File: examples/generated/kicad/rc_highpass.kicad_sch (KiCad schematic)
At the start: 3 parts

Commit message: Attempt to create legible symbols.
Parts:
- C1: symbol examples:CAP -> CAP
- R1: symbol examples:R -> R
- V1: symbol examples:VSOURCE -> VSOURCE
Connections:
- net GND: now also R1.2, V1.1 (E1)
- new net: C1.1, V1.2 (E2)
- new net: C1.2, R1.1
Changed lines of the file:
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@@
     (comment 1 "Generated by mixedsig2cad")
   )
-  (symbol (lib_id "examples:VSOURCE") (at 50.00 55.00 0) (unit 1)
+  (symbol (lib_id "VSOURCE") (at 50.00 55.00 0) (unit 1)
     (in_bom yes) (on_board yes)
     (property "Reference" "V1" (at 50.0 51.19 0)
@@
     )
   )
-  (symbol (lib_id "examples:CAP") (at 95.00 55.00 90) (unit 1)
+  (symbol (lib_id "CAP") (at 95.00 55.00 90) (unit 1)
     (in_bom yes) (on_board yes)
     (property "Reference" "C1" (at 95.0 51.19 0)
@@
     )
   )
-  (symbol (lib_id "examples:R") (at 95.00 90.00 90) (unit 1)
+  (symbol (lib_id "R") (at 95.00 90.00 90) (unit 1)
     (in_bom yes) (on_board yes)
     (property "Reference" "R1" (at 95.0 86.19 0)
@@
     )
   )
-  (symbol (lib_id "examples:GND") (at 38.00 41.38 0) (unit 1)
+  (symbol (lib_id "GND") (at 38.00 41.38 0) (unit 1)
     (in_bom yes) (on_board yes)
     (property "Reference" "#PWR0001" (at 38.0 37.57 0)

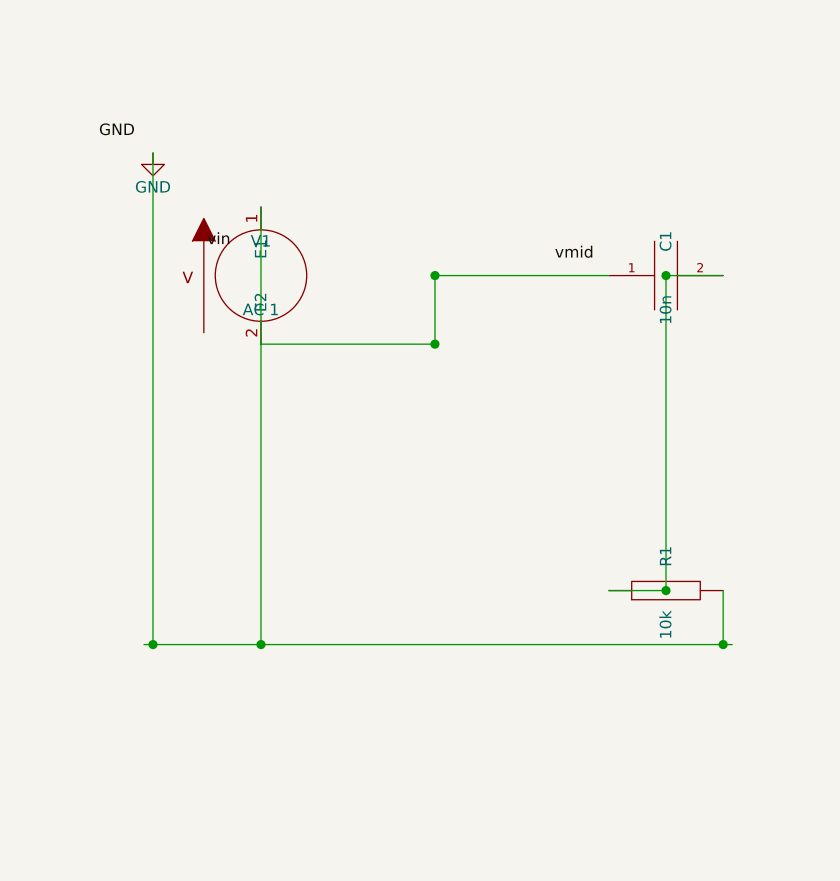
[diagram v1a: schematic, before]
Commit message: Attempt full seperation of circuit concerns into layers.
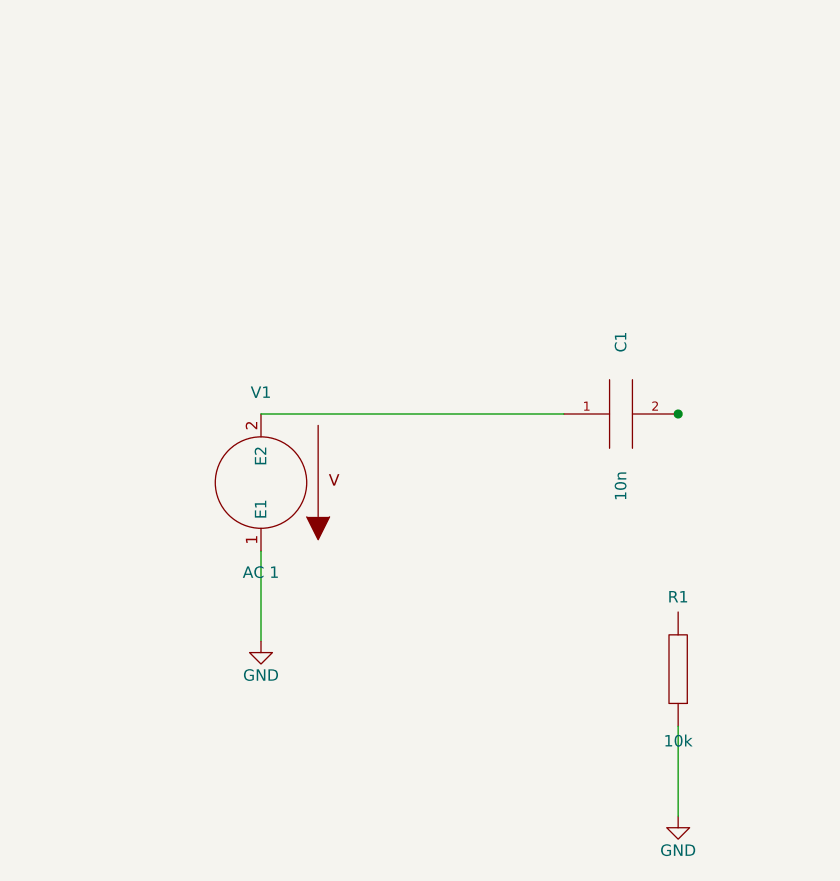
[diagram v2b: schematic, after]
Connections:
- net GND: now also R1.1; no longer R1.2
- net at C1.2: no longer R1.1
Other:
- moved on the sheet: C1, R1, V1
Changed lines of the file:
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@@
   (title_block
     (title "rc_highpass")
-    (date "2026-03-05")
+    (date "2026-03-06")
     (comment 1 "Generated by mixedsig2cad")
   )
-  (symbol (lib_id "VSOURCE") (at 50.00 55.00 0) (unit 1)
+  (symbol (lib_id "VSOURCE") (at 50.00 78.00 180) (unit 1)
     (in_bom yes) (on_board yes)
-    (property "Reference" "V1" (at 50.0 51.19 0)
+    (property "Reference" "V1" (at 50.0 68.0 0)
       (effects (font (size 1.27 1.27)))
     )
-    (property "Value" "AC 1" (at 50.0 58.81 0)
+    (property "Value" "AC 1" (at 50.0 88.0 0)
       (effects (font (size 1.27 1.27)))
     )
@@
     )
   )
-  (symbol (lib_id "CAP") (at 95.00 55.00 90) (unit 1)
+  (symbol (lib_id "CAP") (at 90.00 70.38 90) (unit 1)
     (in_bom yes) (on_board yes)
-    (property "Reference" "C1" (at 95.0 51.19 0)
+    (property "Reference" "C1" (at 90.0 62.379999999999995 0)
       (effects (font (size 1.27 1.27)))
     )
-    (property "Value" "10n" (at 95.0 58.81 0)
+    (property "Value" "10n" (at 90.0 78.38 0)
       (effects (font (size 1.27 1.27)))
     )
@@
     )
   )
-  (symbol (lib_id "R") (at 95.00 90.00 90) (unit 1)
+  (symbol (lib_id "R") (at 96.35 98.73 180) (unit 1)
     (in_bom yes) (on_board yes)
-    (property "Reference" "R1" (at 95.0 86.19 0)
+    (property "Reference" "R1" (at 96.35 90.73 0)
       (effects (font (size 1.27 1.27)))
     )
-    (property "Value" "10k" (at 95.0 93.81 0)
+    (property "Value" "10k" (at 96.35 106.73 0)
       (effects (font (size 1.27 1.27)))
     )
@@
     )
   )
-  (symbol (lib_id "GND") (at 38.00 41.38 0) (unit 1)
+  (symbol (lib_id "GND") (at 50.00 95.62 0) (unit 1)
     (in_bom yes) (on_board yes)
-    (property "Reference" "#PWR0001" (at 38.0 37.57 0)
+    (property "Reference" "#PWR0001" (at 50.0 91.81 0)
       (effects (font (size 1.27 1.27)) hide)
     )
-    (property "Value" "GND" (at 38.0 45.190000000000005 0)
+    (property "Value" "GND" (at 50.0 99.43 0)
       (effects (font (size 1.27 1.27)))
     )
@@
     )
   )
-  (label "GND" (at 32.00 39.88 0)
-    (effects (font (size 1.27 1.27)) (justify left bottom))
+  (symbol (lib_id "GND") (at 96.35 115.08 0) (unit 1)
+    (in_bom yes) (on_board yes)
+    (property "Reference" "#PWR0002" (at 96.35 111.27 0)
+      (effects (font (size 1.27 1.27)) hide)
+    )
+    (property "Value" "GND" (at 96.35 118.89 0)
+      (effects (font (size 1.27 1.27)))
+    )
+    (property "Footprint" "" (at 0 0 0)
+      (effects (font (size 1.27 1.27)) hide)
+    )
+    (property "Datasheet" "" (at 0 0 0)
+      (effects (font (size 1.27 1.27)) hide)
+    )
   )
-  (label "vin" (at 44.00 52.00 0)
-    (effects (font (size 1.27 1.27)) (justify left bottom))
-  )
-  (label "vmid" (at 82.65 53.50 0)
-    (effects (font (size 1.27 1.27)) (justify left bottom))
-  )
-  (wire (pts (xy 37.00 96.00) (xy 102.35 96.00))
+  (wire (pts (xy 50.00 70.38) (xy 83.65 70.38))
     (stroke (width 0) (type solid) (color 0 0 0 0))
   )
-  (wire (pts (xy 50.00 47.38) (xy 50.00 96.00))
+  (wire (pts (xy 50.00 85.62) (xy 50.00 95.62))
     (stroke (width 0) (type solid) (color 0 0 0 0))
   )
-  (wire (pts (xy 101.35 90.00) (xy 101.35 96.00))
+  (wire (pts (xy 96.35 105.08) (xy 96.35 115.08))
     (stroke (width 0) (type solid) (color 0 0 0 0))
   )
-  (wire (pts (xy 38.00 41.38) (xy 38.00 96.00))
-    (stroke (width 0) (type solid) (color 0 0 0 0))
-  )
-  (wire (pts (xy 50.00 62.62) (xy 69.33 62.62))
-    (stroke (width 0) (type solid) (color 0 0 0 0))
-  )
-  (wire (pts (xy 69.33 62.62) (xy 69.33 55.00))
-    (stroke (width 0) (type solid) (color 0 0 0 0))
-  )
-  (wire (pts (xy 69.33 55.00) (xy 88.65 55.00))
-    (stroke (width 0) (type solid) (color 0 0 0 0))
-  )
-  (wire (pts (xy 101.35 55.00) (xy 95.00 55.00))
-    (stroke (width 0) (type solid) (color 0 0 0 0))
-  )
-  (wire (pts (xy 95.00 55.00) (xy 95.00 90.00))
-    (stroke (width 0) (type solid) (color 0 0 0 0))
-  )
-  (wire (pts (xy 95.00 90.00) (xy 88.65 90.00))
-    (stroke (width 0) (type solid) (color 0 0 0 0))
-  )
-  (junction (at 50.00 96.00) (diameter 1.016) (color 0 0 0 0))
-  (junction (at 101.35 96.00) (diameter 1.016) (color 0 0 0 0))
-  (junction (at 38.00 96.00) (diameter 1.016) (color 0 0 0 0))
-  (junction (at 69.33 62.62) (diameter 1.016) (color 0 0 0 0))
-  (junction (at 69.33 55.00) (diameter 1.016) (color 0 0 0 0))
-  (junction (at 95.00 55.00) (diameter 1.016) (color 0 0 0 0))
-  (junction (at 95.00 90.00) (diameter 1.016) (color 0 0 0 0))
+  (junction (at 96.35 70.38) (diameter 1.016) (color 0 0 0 0))
   (sheet_instances
     (path "/" (page "1"))
@@
     (path "/58c843b2-6559-5058-b688-d947388eea66" (reference "C1") (unit 1) (value "10n") (footprint ""))
     (path "/ded07918-9cee-5a7e-a275-1ccd4f0b81cb" (reference "R1") (unit 1) (value "10k") (footprint ""))
-    (path "/d8da4189-b640-53d1-b8a8-ab7b6ff38be4" (reference "#PWR0001") (unit 1) (value "GND") (footprint ""))
+    (path "/d76d2626-14f8-5e35-8eaa-916a5b195b2f" (reference "#PWR0001") (unit 1) (value "GND") (footprint ""))
+    (path "/866988e1-0e40-5667-846e-d709fa13875c" (reference "#PWR0002") (unit 1) (value "GND") (footprint ""))
   )
 )

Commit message: Add checks for connectivity.
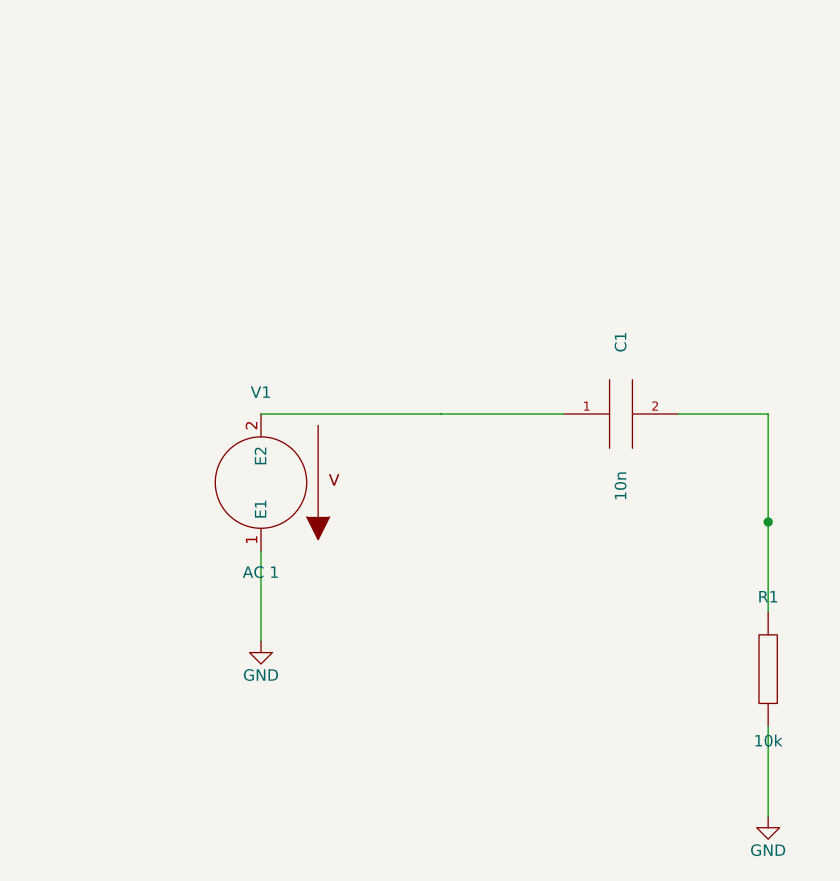
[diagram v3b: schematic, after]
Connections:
- net at C1.2: now also R1.2
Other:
- moved on the sheet: R1
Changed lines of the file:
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@@
     )
   )
-  (symbol (lib_id "R") (at 96.35 98.73 180) (unit 1)
+  (symbol (lib_id "R") (at 106.35 98.73 180) (unit 1)
     (in_bom yes) (on_board yes)
-    (property "Reference" "R1" (at 96.35 90.73 0)
+    (property "Reference" "R1" (at 106.35 90.73 0)
       (effects (font (size 1.27 1.27)))
     )
-    (property "Value" "10k" (at 96.35 106.73 0)
+    (property "Value" "10k" (at 106.35 106.73 0)
       (effects (font (size 1.27 1.27)))
     )
@@
     )
   )
-  (symbol (lib_id "GND") (at 96.35 115.08 0) (unit 1)
+  (symbol (lib_id "GND") (at 106.35 115.08 0) (unit 1)
     (in_bom yes) (on_board yes)
-    (property "Reference" "#PWR0002" (at 96.35 111.27 0)
+    (property "Reference" "#PWR0002" (at 106.35 111.27 0)
       (effects (font (size 1.27 1.27)) hide)
     )
-    (property "Value" "GND" (at 96.35 118.89 0)
+    (property "Value" "GND" (at 106.35 118.89 0)
       (effects (font (size 1.27 1.27)))
     )
@@
     )
   )
-  (wire (pts (xy 50.00 70.38) (xy 83.65 70.38))
+  (wire (pts (xy 50.00 70.38) (xy 70.00 70.38))
+    (stroke (width 0) (type solid) (color 0 0 0 0))
+  )
+  (wire (pts (xy 83.65 70.38) (xy 70.00 70.38))
+    (stroke (width 0) (type solid) (color 0 0 0 0))
+  )
+  (wire (pts (xy 96.35 70.38) (xy 106.35 70.38))
+    (stroke (width 0) (type solid) (color 0 0 0 0))
+  )
+  (wire (pts (xy 106.35 70.38) (xy 106.35 82.38))
+    (stroke (width 0) (type solid) (color 0 0 0 0))
+  )
+  (wire (pts (xy 106.35 92.38) (xy 106.35 82.38))
     (stroke (width 0) (type solid) (color 0 0 0 0))
   )
@@
     (stroke (width 0) (type solid) (color 0 0 0 0))
   )
-  (wire (pts (xy 96.35 105.08) (xy 96.35 115.08))
+  (wire (pts (xy 106.35 105.08) (xy 106.35 115.08))
     (stroke (width 0) (type solid) (color 0 0 0 0))
   )
-  (junction (at 96.35 70.38) (diameter 1.016) (color 0 0 0 0))
+  (junction (at 106.35 82.38) (diameter 1.016) (color 0 0 0 0))
   (sheet_instances
     (path "/" (page "1"))

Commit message: Attempt to correct strange wiring.
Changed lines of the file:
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@@
     )
   )
-  (wire (pts (xy 50.00 70.38) (xy 70.00 70.38))
+  (wire (pts (xy 50.00 70.38) (xy 83.65 70.38))
     (stroke (width 0) (type solid) (color 0 0 0 0))
   )
-  (wire (pts (xy 83.65 70.38) (xy 70.00 70.38))
-    (stroke (width 0) (type solid) (color 0 0 0 0))
-  )

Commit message: Attempt shape and wiring fixes again.
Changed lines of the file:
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@@
     (stroke (width 0) (type solid) (color 0 0 0 0))
   )
-  (wire (pts (xy 50.00 85.62) (xy 50.00 95.62))
+  (wire (pts (xy 50.00 85.62) (xy 50.00 87.50))
     (stroke (width 0) (type solid) (color 0 0 0 0))
   )
-  (wire (pts (xy 106.35 105.08) (xy 106.35 115.08))
+  (wire (pts (xy 50.00 87.50) (xy 56.00 87.50))
     (stroke (width 0) (type solid) (color 0 0 0 0))
   )
+  (wire (pts (xy 56.00 87.50) (xy 56.00 95.62))
+    (stroke (width 0) (type solid) (color 0 0 0 0))
+  )
+  (wire (pts (xy 56.00 95.62) (xy 50.00 95.62))
+    (stroke (width 0) (type solid) (color 0 0 0 0))
+  )
+  (wire (pts (xy 106.35 105.08) (xy 106.35 107.23))
+    (stroke (width 0) (type solid) (color 0 0 0 0))
+  )
+  (wire (pts (xy 106.35 107.23) (xy 112.35 107.23))
+    (stroke (width 0) (type solid) (color 0 0 0 0))
+  )
+  (wire (pts (xy 112.35 107.23) (xy 112.35 115.08))
+    (stroke (width 0) (type solid) (color 0 0 0 0))
+  )
+  (wire (pts (xy 112.35 115.08) (xy 106.35 115.08))
+    (stroke (width 0) (type solid) (color 0 0 0 0))
+  )

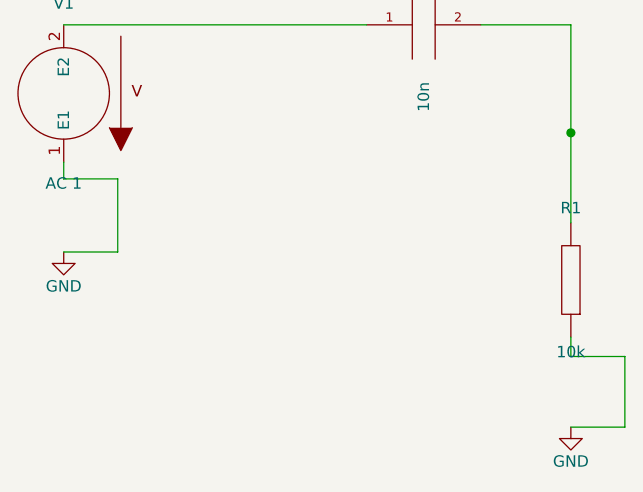
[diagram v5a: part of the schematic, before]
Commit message: Attempt to fix kinking and terminal direction issuses.
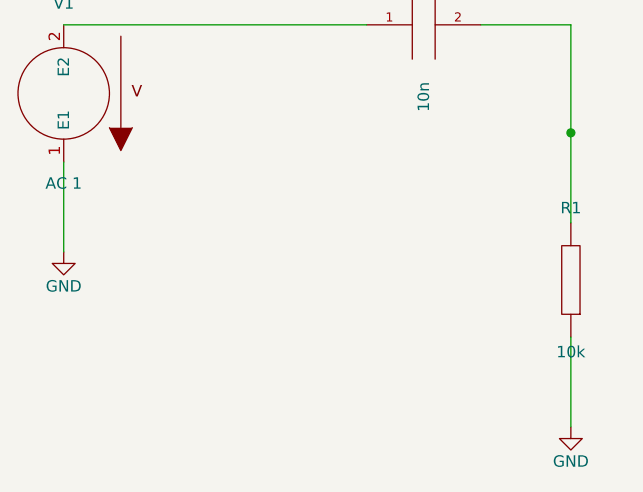
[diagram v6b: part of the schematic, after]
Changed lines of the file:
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@@
     (stroke (width 0) (type solid) (color 0 0 0 0))
   )
-  (wire (pts (xy 50.00 85.62) (xy 50.00 87.50))
+  (wire (pts (xy 50.00 85.62) (xy 50.00 95.62))
     (stroke (width 0) (type solid) (color 0 0 0 0))
   )
-  (wire (pts (xy 50.00 87.50) (xy 56.00 87.50))
+  (wire (pts (xy 106.35 105.08) (xy 106.35 115.08))
     (stroke (width 0) (type solid) (color 0 0 0 0))
   )
-  (wire (pts (xy 56.00 87.50) (xy 56.00 95.62))
-    (stroke (width 0) (type solid) (color 0 0 0 0))
-  )
-  (wire (pts (xy 56.00 95.62) (xy 50.00 95.62))
-    (stroke (width 0) (type solid) (color 0 0 0 0))
-  )
-  (wire (pts (xy 106.35 105.08) (xy 106.35 107.23))
-    (stroke (width 0) (type solid) (color 0 0 0 0))
-  )
-  (wire (pts (xy 106.35 107.23) (xy 112.35 107.23))
-    (stroke (width 0) (type solid) (color 0 0 0 0))
-  )
-  (wire (pts (xy 112.35 107.23) (xy 112.35 115.08))
-    (stroke (width 0) (type solid) (color 0 0 0 0))
-  )
-  (wire (pts (xy 112.35 115.08) (xy 106.35 115.08))
-    (stroke (width 0) (type solid) (color 0 0 0 0))
-  )

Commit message: Attempt to fix more terminal issues.
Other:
- moved on the sheet: C1, R1, V1
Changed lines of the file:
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@@
     (comment 1 "Generated by mixedsig2cad")
   )
-  (symbol (lib_id "VSOURCE") (at 50.00 78.00 180) (unit 1)
+  (symbol (lib_id "VSOURCE") (at 56.00 86.00 180) (unit 1)
     (in_bom yes) (on_board yes)
-    (property "Reference" "V1" (at 50.0 68.0 0)
+    (property "Reference" "V1" (at 56.0 76.0 0)
       (effects (font (size 1.27 1.27)))
     )
-    (property "Value" "AC 1" (at 50.0 88.0 0)
+    (property "Value" "AC 1" (at 56.0 96.0 0)
       (effects (font (size 1.27 1.27)))
     )
@@
     )
   )
-  (symbol (lib_id "CAP") (at 90.00 70.38 90) (unit 1)
+  (symbol (lib_id "GND") (at 56.00 105.62 0) (unit 1)
     (in_bom yes) (on_board yes)
-    (property "Reference" "C1" (at 90.0 62.379999999999995 0)
-      (effects (font (size 1.27 1.27)))
+    (property "Reference" "#PWR0001" (at 56.0 101.81 0)
+      (effects (font (size 1.27 1.27)) hide)
     )
-    (property "Value" "10n" (at 90.0 78.38 0)
+    (property "Value" "GND" (at 56.0 109.43 0)
       (effects (font (size 1.27 1.27)))
     )
@@
     )
   )
-  (symbol (lib_id "R") (at 106.35 98.73 180) (unit 1)
+  (symbol (lib_id "CAP") (at 90.00 78.00 90) (unit 1)
     (in_bom yes) (on_board yes)
-    (property "Reference" "R1" (at 106.35 90.73 0)
+    (property "Reference" "C1" (at 90.0 70.0 0)
       (effects (font (size 1.27 1.27)))
     )
-    (property "Value" "10k" (at 106.35 106.73 0)
+    (property "Value" "10n" (at 90.0 86.0 0)
       (effects (font (size 1.27 1.27)))
     )
@@
     )
   )
-  (symbol (lib_id "GND") (at 50.00 95.62 0) (unit 1)
+  (symbol (lib_id "R") (at 96.35 96.35 180) (unit 1)
     (in_bom yes) (on_board yes)
-    (property "Reference" "#PWR0001" (at 50.0 91.81 0)
-      (effects (font (size 1.27 1.27)) hide)
+    (property "Reference" "R1" (at 96.35 88.35 0)
+      (effects (font (size 1.27 1.27)))
     )
-    (property "Value" "GND" (at 50.0 99.43 0)
+    (property "Value" "10k" (at 96.35 104.35 0)
       (effects (font (size 1.27 1.27)))
     )
@@
     )
   )
-  (symbol (lib_id "GND") (at 106.35 115.08 0) (unit 1)
+  (symbol (lib_id "GND") (at 96.35 114.70 0) (unit 1)
     (in_bom yes) (on_board yes)
-    (property "Reference" "#PWR0002" (at 106.35 111.27 0)
+    (property "Reference" "#PWR0002" (at 96.35 110.89 0)
       (effects (font (size 1.27 1.27)) hide)
     )
-    (property "Value" "GND" (at 106.35 118.89 0)
+    (property "Value" "GND" (at 96.35 118.51 0)
       (effects (font (size 1.27 1.27)))
     )
@@
     )
   )
-  (wire (pts (xy 50.00 70.38) (xy 83.65 70.38))
+  (wire (pts (xy 96.35 102.70) (xy 96.35 114.70))
     (stroke (width 0) (type solid) (color 0 0 0 0))
   )
-  (wire (pts (xy 96.35 70.38) (xy 106.35 70.38))
+  (wire (pts (xy 56.00 93.62) (xy 56.00 105.62))
     (stroke (width 0) (type solid) (color 0 0 0 0))
   )
-  (wire (pts (xy 106.35 70.38) (xy 106.35 82.38))
+  (wire (pts (xy 56.00 78.38) (xy 56.00 78.00))
     (stroke (width 0) (type solid) (color 0 0 0 0))
   )
-  (wire (pts (xy 106.35 92.38) (xy 106.35 82.38))
+  (wire (pts (xy 56.00 78.00) (xy 83.65 78.00))
     (stroke (width 0) (type solid) (color 0 0 0 0))
   )
-  (wire (pts (xy 50.00 85.62) (xy 50.00 95.62))
+  (wire (pts (xy 96.35 78.00) (xy 96.35 90.00))
     (stroke (width 0) (type solid) (color 0 0 0 0))
   )
-  (wire (pts (xy 106.35 105.08) (xy 106.35 115.08))
-    (stroke (width 0) (type solid) (color 0 0 0 0))
-  )
-  (junction (at 106.35 82.38) (diameter 1.016) (color 0 0 0 0))
   (sheet_instances
     (path "/" (page "1"))
@@
   (symbol_instances
     (path "/236c4ed6-19b0-5092-bdb2-caacc762cc72" (reference "V1") (unit 1) (value "AC 1") (footprint ""))
+    (path "/d76d2626-14f8-5e35-8eaa-916a5b195b2f" (reference "#PWR0001") (unit 1) (value "GND") (footprint ""))
     (path "/58c843b2-6559-5058-b688-d947388eea66" (reference "C1") (unit 1) (value "10n") (footprint ""))
     (path "/ded07918-9cee-5a7e-a275-1ccd4f0b81cb" (reference "R1") (unit 1) (value "10k") (footprint ""))
-    (path "/d76d2626-14f8-5e35-8eaa-916a5b195b2f" (reference "#PWR0001") (unit 1) (value "GND") (footprint ""))
     (path "/866988e1-0e40-5667-846e-d709fa13875c" (reference "#PWR0002") (unit 1) (value "GND") (footprint ""))
   )
